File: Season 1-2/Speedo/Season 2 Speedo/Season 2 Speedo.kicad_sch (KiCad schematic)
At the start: 60 parts, among them U1 Pico

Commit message: Progress on speedo pcb
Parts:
- added Q1: DMG2305UX, Package_TO_SOT_SMD_AKL:SOT-23, symbol PCM_Transistor_MOSFET_AKL:DMG2305UX
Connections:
- net GND: now also U1.13 (GND), U1.18 (GND), U1.23 (GND), U1.28 (GND), U1.3 (GND), U1.33 (AGND), U1.38 (GND), U1.8 (GND)

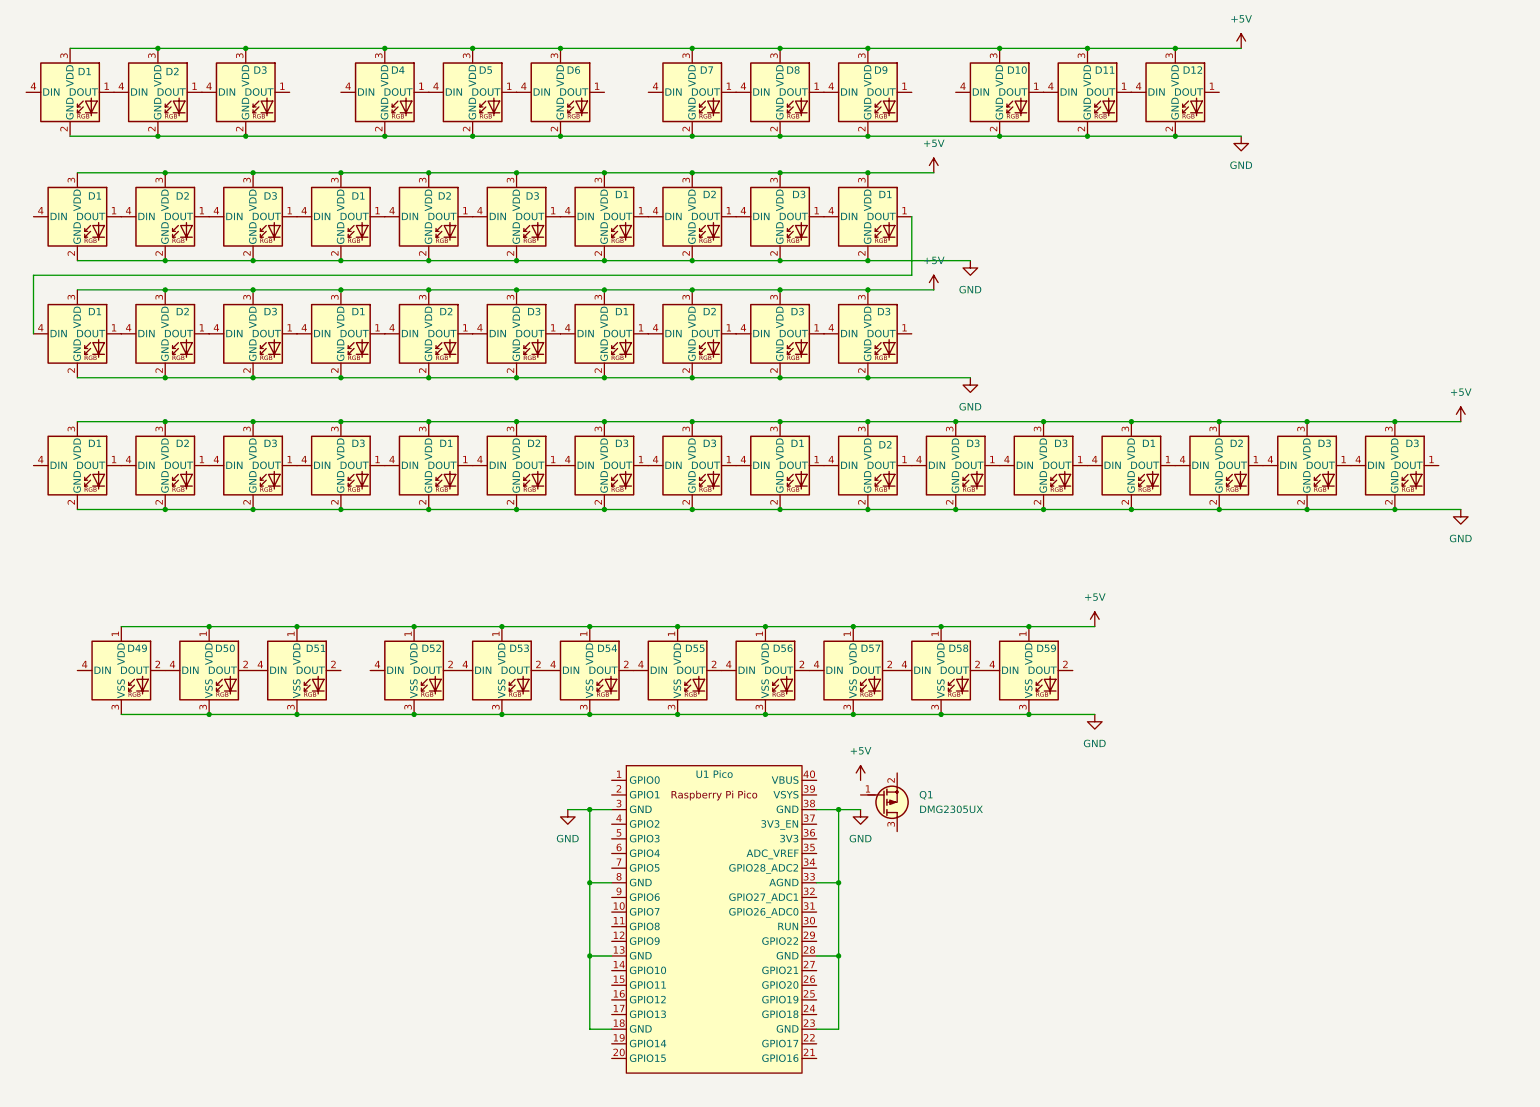
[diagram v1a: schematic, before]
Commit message: Season 1/2 Speedo board updates
Season 1/2 Speedo board mostly complete, a few modifications still pending.
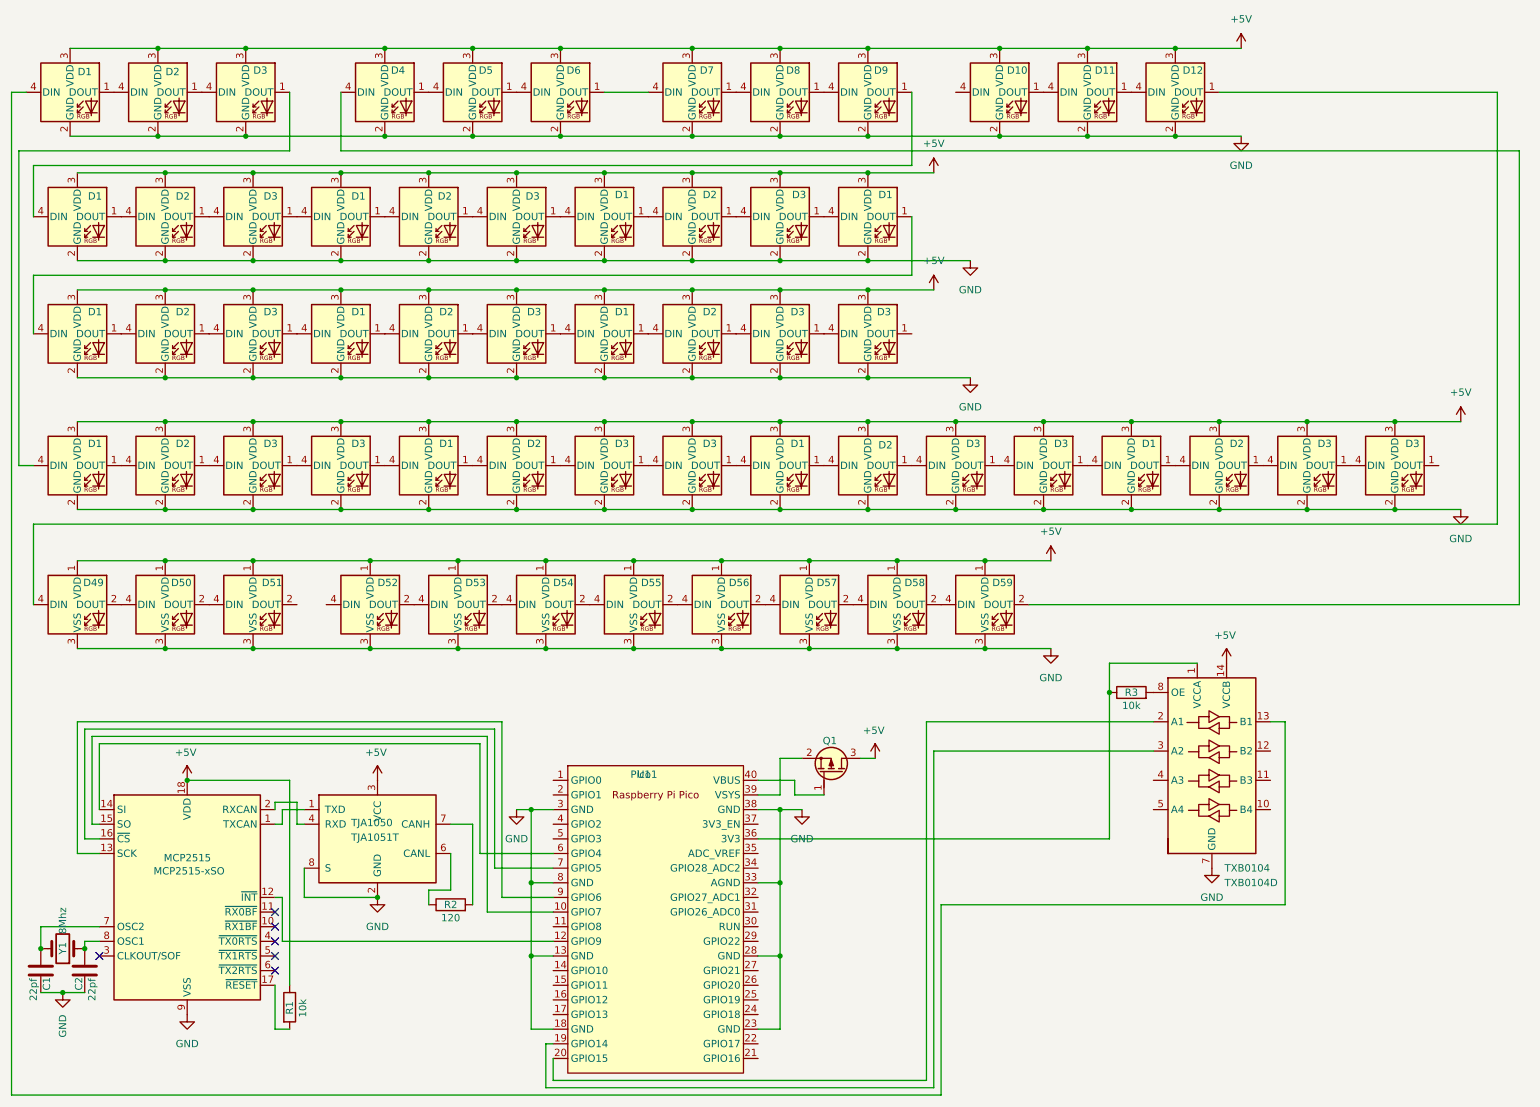
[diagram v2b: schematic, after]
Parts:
- added C1, C2: 22pf, Capacitor_SMD:C_0805_2012Metric, symbol PCM_Capacitor_AKL:C_0805
- added MCP2515: MCP2515-xSO, Package_SO:SOIC-18W_7.5x11.6mm_P1.27mm, symbol Interface_CAN_LIN:MCP2515-xSO
- added R1, R3: 10k, PCM_Resistor_SMD_AKL:R_0805_2012Metric_Pad1.15x1.40mm, symbol PCM_Resistor_AKL:R_0805
- added R2: 120, PCM_Resistor_SMD_AKL:R_0805_2012Metric_Pad1.15x1.40mm, symbol PCM_Resistor_AKL:R_0805
- added TJA1050: TJA1051T, Package_SO:SOIC-8_3.9x4.9mm_P1.27mm, symbol Interface_CAN_LIN:TJA1051T
- added TXB0104: TXB0104D, Package_SO:SOIC-14_3.9x8.7mm_P1.27mm, symbol Logic_LevelTranslator:TXB0104D
- added Y1: 8Mhz, Crystal:Crystal_HC49-U_Vertical, symbol Device:Crystal
- Q1: footprint Package_TO_SOT_SMD_AKL:SOT-23 -> footprints:SOT91P240X110-3N_DMG2305UX-7
- U1: value Pico -> Pico1
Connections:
- net +5V: now also Q1.3 (D), MCP2515.18 (VDD), R1.1, TJA1050.3 (VCC), TXB0104.14 (VCCB)
- net GND: now also C1.1, C2.1, MCP2515.9 (VSS), TJA1050.2 (GND), TJA1050.8 (S), TXB0104.7 (GND)
- net at D1.4 (DIN): now also D9.1 (DOUT)
- net at D7.4 (DIN): now also D6.1 (DOUT)
- net at D1.4 (DIN): now also D3.1 (DOUT)
- net at D49.4 (DIN): now also D12.1 (DOUT)
- net at Q1.1 (G): now also U1.40 (VBUS)
- net at Q1.2 (S): now also U1.39 (VSYS)
- net at D1.4 (DIN): now also TXB0104.13 (B1)
- net at U1.10 (GPIO7): now also MCP2515.15 (SO)
- net at U1.12 (GPIO9): now also MCP2515.12 (~{INT})
- net at U1.19 (GPIO14): now also TXB0104.3 (A2)
- net at U1.20 (GPIO15): now also TXB0104.2 (A1)
- net at U1.36 (3V3): now also R3.1, TXB0104.1 (VCCA)
- net at U1.6 (GPIO4): now also MCP2515.14 (SI)
- net at U1.7 (GPIO5): now also MCP2515.16 (~{CS})
- net at U1.9 (GPIO6): now also MCP2515.13 (SCK)
- net at D4.4 (DIN): now also D59.2 (DOUT)
- new net: R3.2, TXB0104.8 (OE)
- new net: C2.2, MCP2515.8 (OSC1), Y1.1
- new net: C1.2, MCP2515.7 (OSC2), Y1.2
- new net: MCP2515.1 (TXCAN), TJA1050.1 (TXD)
- new net: MCP2515.17 (~{RESET}), R1.2
- new net: MCP2515.2 (RXCAN), TJA1050.4 (RXD)
- new net: R2.1, TJA1050.6 (CANL)
- new net: R2.2, TJA1050.7 (CANH)
- no-connect marks 0 -> 6
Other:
- moved on the sheet: D49, D50, D51, D52, D53, D54, D55, D56, D57, D58, D59, Q1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
